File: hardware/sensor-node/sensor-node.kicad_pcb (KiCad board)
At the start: 2 copper layers, 70 x 70 mm, 46 parts, among them J1 Conn_ARM_JTAG_SWD_10, U1 AAT1217, U2 TPS27081A, U3 SHT31-DIS, U4 24LC32, U5 TSD305, U6 ADG633YCP, U7 TSV911RILT, U8 RFM95W, U9 STM32L412KB

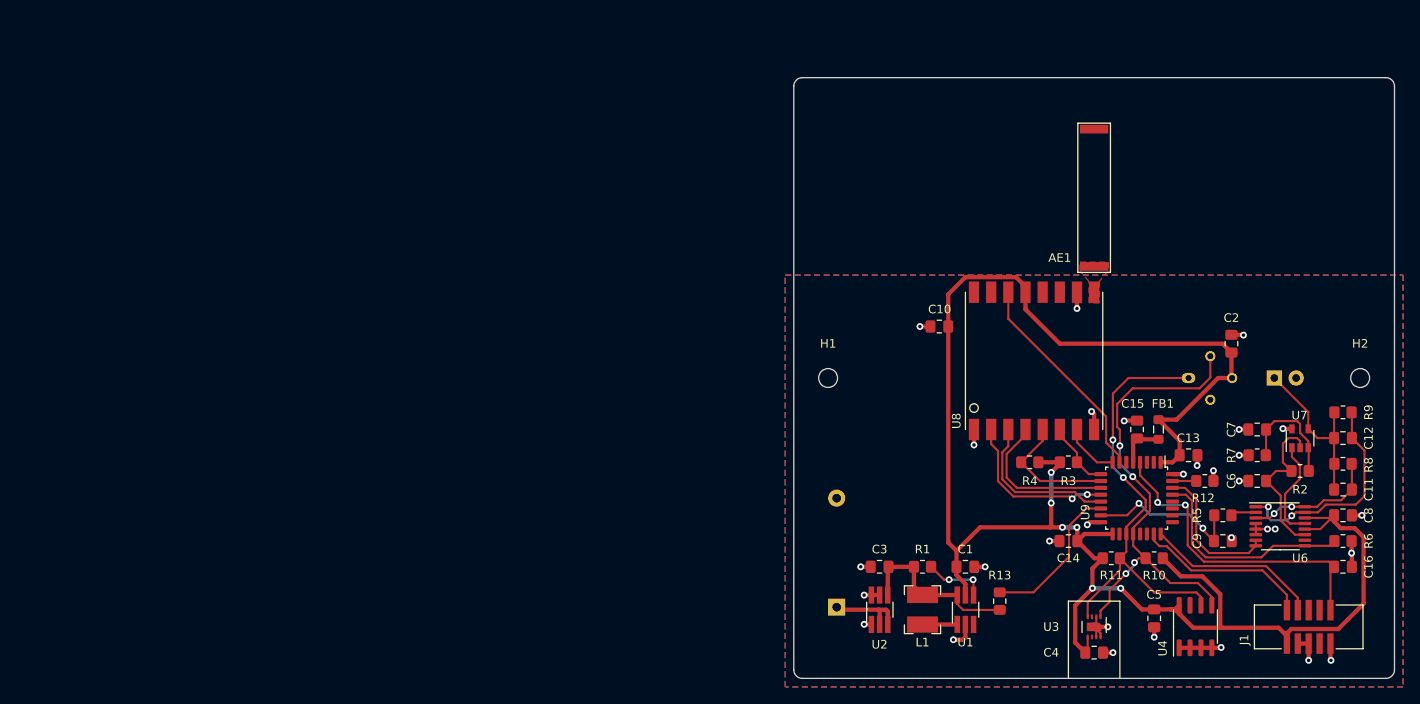
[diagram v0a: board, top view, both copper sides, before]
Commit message: Update PCB, add debugging printouts to application
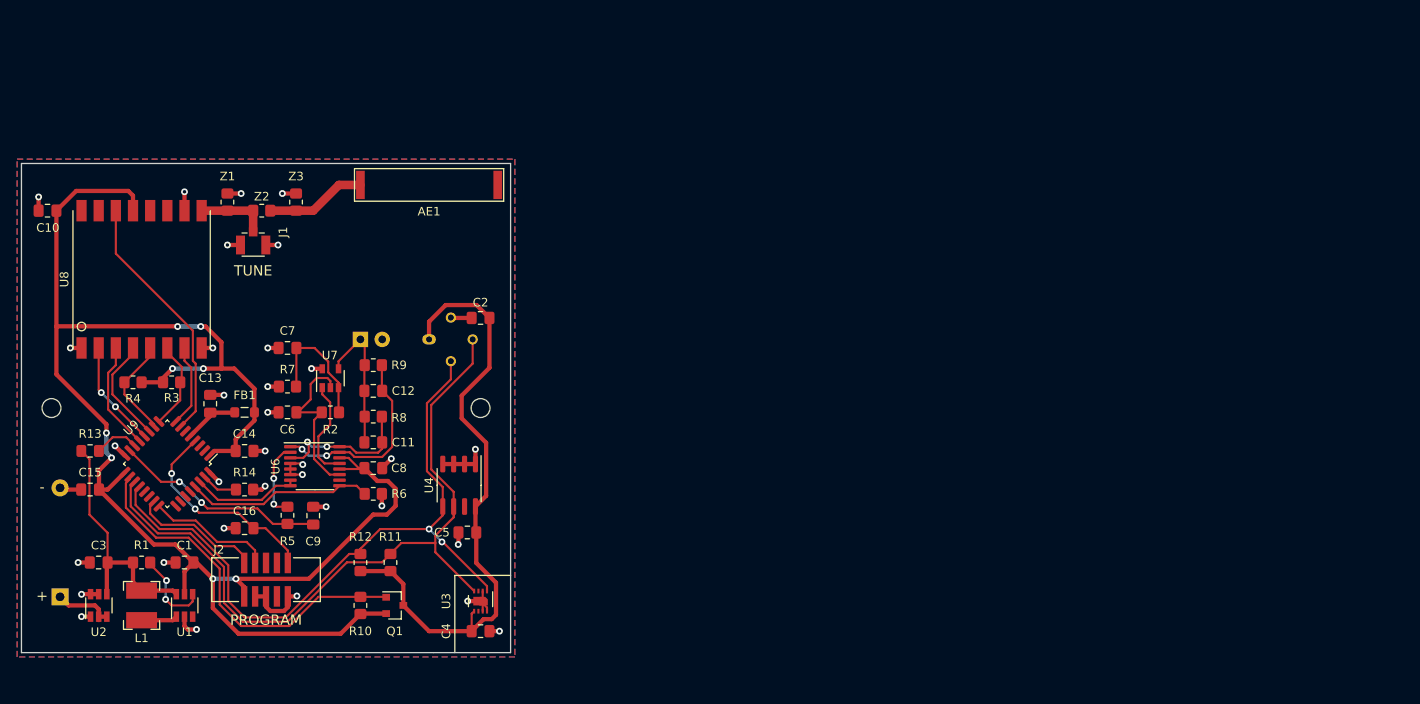
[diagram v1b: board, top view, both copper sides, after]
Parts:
- added J1: Conn_Coaxial, my-footprints-library:CONUFL001-SMD, F.Cu at (117.0, 69.5)
- added Q1: Q_PMOS_DGS, Package_TO_SOT_SMD:SOT-23, F.Cu at (133.5, 111.5)
- added R10: 100k, Resistor_SMD:R_0805_2012Metric_Pad1.20x1.40mm_HandSolder, F.Cu at (129.5, 111.5)
- added Z1: Z, Resistor_SMD:R_0805_2012Metric_Pad1.20x1.40mm_HandSolder, F.Cu at (114.0, 64.5)
- added Z2: Z, Resistor_SMD:R_0805_2012Metric_Pad1.20x1.40mm_HandSolder, F.Cu at (118.0, 65.5)
- added Z3: Z, Resistor_SMD:R_0805_2012Metric_Pad1.20x1.40mm_HandSolder, F.Cu at (122.0, 64.5)
- U1, U2: footprint Package_TO_SOT_SMD:TSOT-23-6_HandSoldering -> Package_TO_SOT_SMD:TSOT-23-6
- U5: value TSD305 -> MLX90614; footprint Package_TO_SOT_THT:TO-5-4_Window -> Package_TO_SOT_THT:TO-39-4
- moved C16 128.1 mm to (116.0, 102.5), turned to 180 degrees
- moved J2 121.6 mm to (118.5, 108.5)
- moved C15 114.2 mm to (98.0, 98.0)
- moved C7 113.4 mm to (121.0, 81.5)
- moved C6 113.3 mm to (121.0, 89.0)
- moved R7 113.3 mm to (121.0, 86.0)
- moved U7 113.2 mm to (126.0, 85.0)
- moved R2 113.2 mm to (126.0, 89.0)
- moved C11 113.1 mm to (131.0, 92.5)
- moved C12 113.1 mm to (131.0, 86.5)
- moved C8 113.1 mm to (131.0, 95.5)
- moved R6 113.1 mm to (131.0, 98.5)
- moved R8 113.1 mm to (131.0, 89.5)
- moved R9 113.1 mm to (131.0, 83.5)
- moved U9 113.0 mm to (107.0, 95.0), turned to 225 degrees
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- renumbered C15 to C13, C13 to C14, C14 to C15, J1 to J2, R10 to R11, R11 to R12, R12 to R14
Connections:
- C2 pad 1: +3V3 -> VI2C
- C4 pad 1: +3V3 -> VI2C
- C5 pad 1: +3V3 -> VI2C
- R11 pad 1: +3V3 -> VI2C
- R11 pad 2: SDA -> SCL
- R12 pad 1: +3V3 -> VI2C
- R12 pad 2: SCL -> SDA
- U3 pad 5: +3V3 -> VI2C
- U4 pad 8: +3V3 -> VI2C
- U5 pad 1: SCL -> VI2C
- U5 pad 2: SDA -> GND
- U5 pad 3: +3V3 -> SCL
- U5 pad 4: GND -> SDA
- U8 pad 9: Net-(AE1-Pad1) -> Net-(J1-Pad1)
- U9 pad 18: Net-(U9-Pad18) -> I2C_ENABLE
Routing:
- net VI2C: track 0.00 -> 72.5 mm
- net I2C_ENABLE: track 0.00 -> 43.7 mm
- net SCL: track 52.2 -> 86.5 mm, vias 2 -> 0
- net +3V3: track 218.7 -> 188.5 mm, vias 6 -> 8
- net SDA: track 55.6 -> 81.2 mm, vias 4 -> 2
- net GND: track 54.9 -> 70.5 mm, vias 31 -> 33
- net Net-(R13-Pad2): track 17.9 -> 5.25 mm
- net NRST: track 37.0 -> 24.4 mm
- net Net-(AE1-Pad1): track 0.00 -> 11.7 mm
- net Net-(J1-Pad1): track 0.00 -> 8.47 mm
- net VIN_SENSE: track 20.3 -> 28.5 mm
- net MISO: track 19.4 -> 12.5 mm
- net PHOTO_SENSE: track 18.9 -> 24.9 mm
- net MOSI: track 18.6 -> 12.7 mm
- net SWCLK: track 20.5 -> 14.8 mm
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- removed copper zone on F.Cu, net Net-(AE1-Pad1)
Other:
- board size 70 x 70 mm -> 57 x 57 mm
- board text added: "+"
- board text added: "-"
- board text added: "PROGRAM"
- board text added: "TUNE"

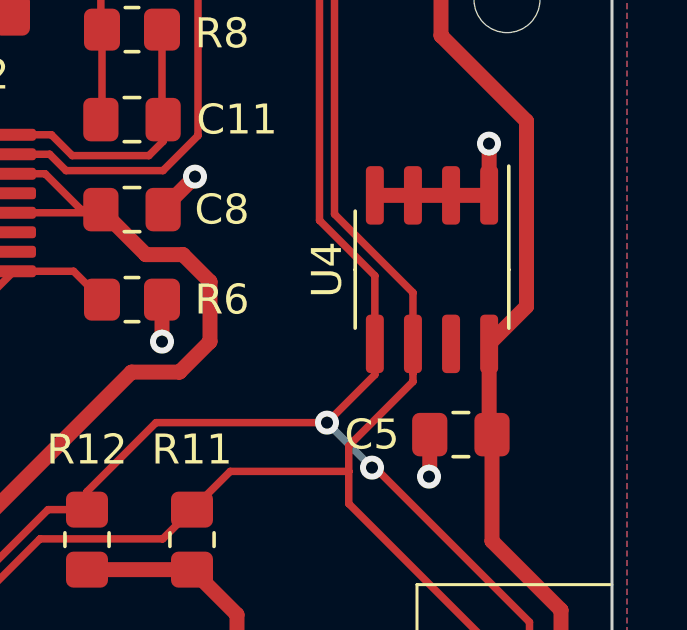
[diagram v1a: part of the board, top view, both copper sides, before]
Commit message: Fix timeouts for systick overflow handling
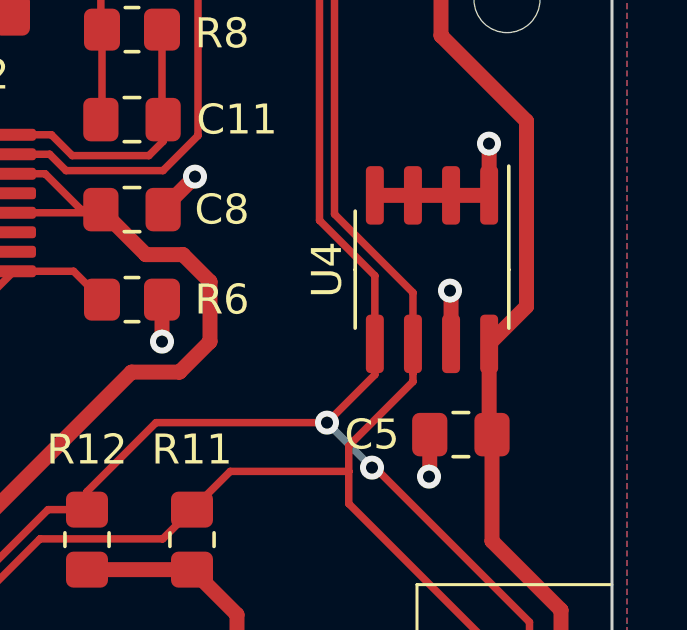
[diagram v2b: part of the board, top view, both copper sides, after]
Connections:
- U4 pad 7: Net-(U4-Pad7) -> GND
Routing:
- net GND: track 70.5 -> 72.3 mm, vias 33 -> 34

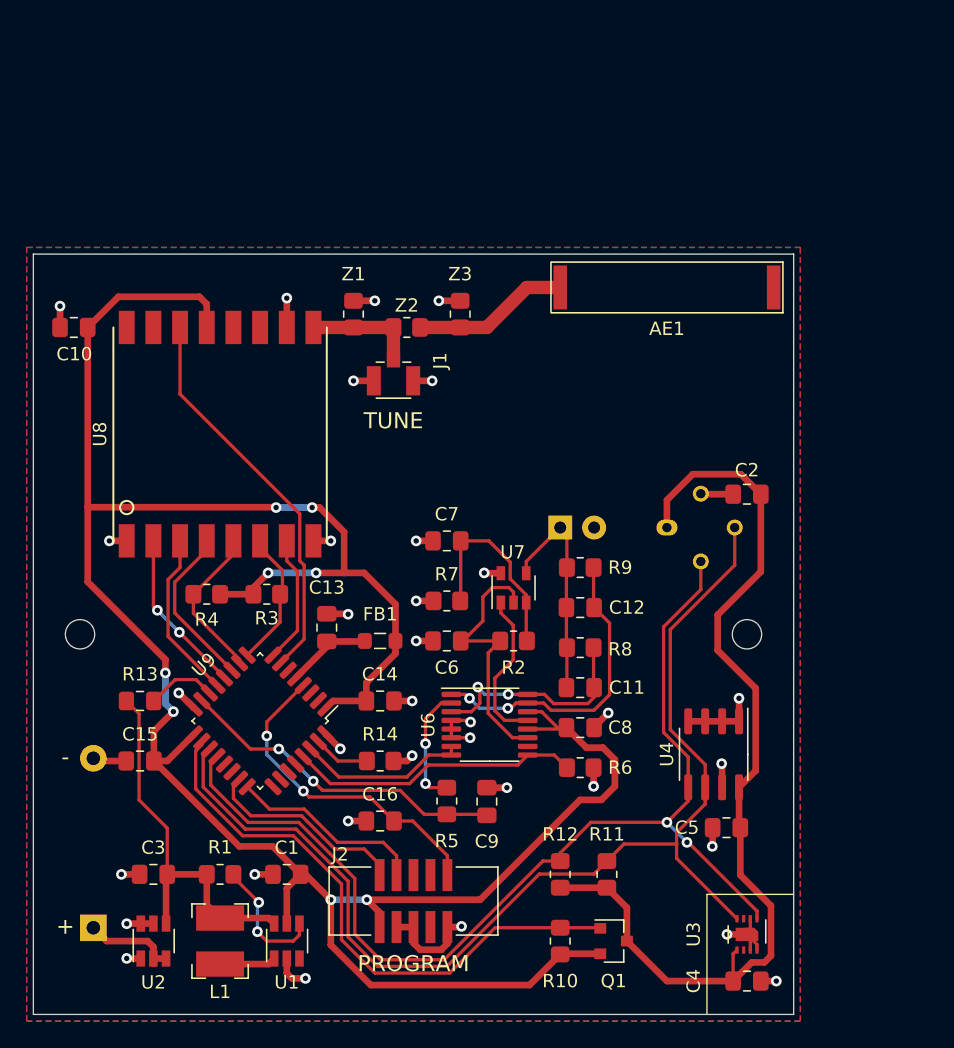
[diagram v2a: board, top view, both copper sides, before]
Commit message: Update PCB for enclosure
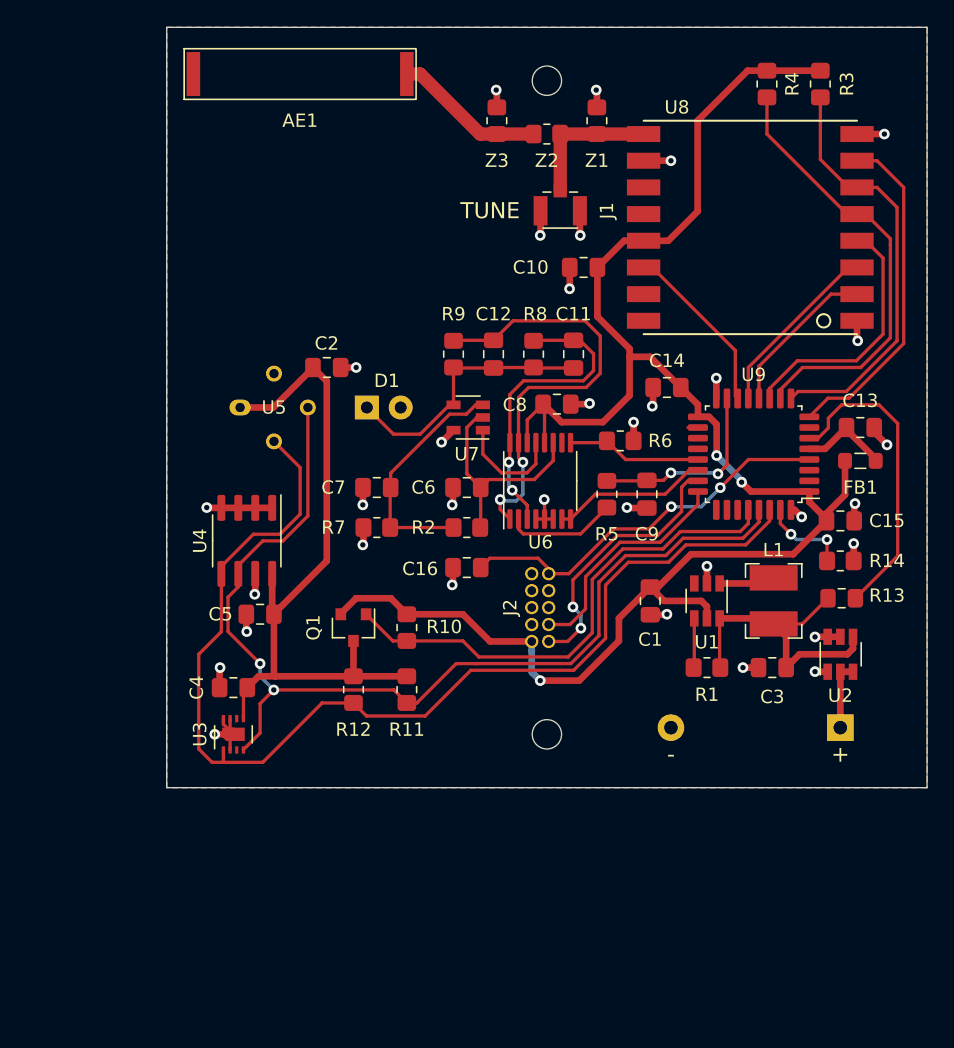
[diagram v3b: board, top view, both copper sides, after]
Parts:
- FB1: value Ferrite_Bead_Small -> WE 742792040
- J1: value Conn_Coaxial -> CONUFL001-SMD-T
- J2: footprint my-footprints-library:Amphenol_FCI_ShroudedSocket_2x05_P1.27mm_Vertical_SMD -> my-footprints-library:SHF-105-01-L-D-TH; moved to B.Cu
- Q1: value Q_PMOS_DGS -> PMV250EPEA
- moved BT1 58.0 mm to (150.5, 95.5), turned to 90 degrees
- moved R4 56.8 mm to (145.0, 47.2), turned to 270 degrees
- moved R3 56.4 mm to (149.0, 47.2), turned to 270 degrees
- moved U2 55.8 mm to (150.5, 90.0)
- moved C15 55.5 mm to (150.5, 80.0), turned to 0 degrees
- moved R13 53.2 mm to (150.6, 85.8)
- moved C3 48.9 mm to (145.4, 91.0)
- moved L1 48.7 mm to (145.5, 86.0), turned to 270 degrees
- moved C4 44.3 mm to (105.0, 92.5), turned to 180 degrees
- moved H2 44.1 mm to (128.5, 47.0)
- moved C13 42.7 mm to (152.0, 73.0), turned to 0 degrees
- moved U8 42.7 mm to (143.8, 58.0), turned to 180 degrees
- moved U9 42.1 mm to (144.0, 75.0), turned to 180 degrees
- moved U3 41.3 mm to (105.0, 96.0), turned to 90 degrees
- moved U1 40.5 mm to (140.5, 86.0), turned to 270 degrees
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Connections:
- U9 pad 14: Net-(R13-Pad2) -> RFM95_IRQ
- U9 pad 18: I2C_ENABLE -> Net-(U9-Pad18)
- U9 pad 19: SCL -> Net-(U9-Pad19)
- U9 pad 20: SDA -> Net-(U9-Pad20)
- U9 pad 21: Net-(U9-Pad21) -> PHOTO_ENABLE
- U9 pad 22: Net-(U9-Pad22) -> PHOTO_SWITCH
- U9 pad 28: Net-(U9-Pad28) -> I2C_ENABLE
- U9 pad 29: PHOTO_ENABLE -> SCL
- U9 pad 30: PHOTO_SWITCH -> SDA
- U9 pad 6: Net-(U9-Pad6) -> Net-(R13-Pad2)
- U9 pad 7: RFM95_IRQ -> Net-(U9-Pad7)
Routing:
- net +3V3: track 188.5 -> 131.6 mm, vias 8 -> 3
- net RFM95_NRST: track 10.4 -> 31.6 mm
- net RFM95_NSS: track 12.4 -> 33.2 mm
- net VI2C: track 72.5 -> 52.5 mm
- net Net-(R13-Pad2): track 5.25 -> 23.1 mm
- net RFM95_IRQ: track 29.7 -> 13.1 mm
- net RFM95_DIO5: track 9.66 -> 25.4 mm
- net GND: track 72.3 -> 58.1 mm
- net PHOTO_ENABLE: track 21.9 -> 10.2 mm
- net PHOTO_SENSE: track 24.9 -> 14.5 mm
- net Net-(C12-Pad2): track 23.2 -> 32.9 mm
- net SCL: track 86.5 -> 77.1 mm, vias 0 -> 2
- net SCK: track 12.5 -> 19.1 mm
- net Net-(C11-Pad2): track 16.8 -> 23.2 mm
- net Net-(R1-Pad2): track 10.0 -> 3.71 mm, vias 2 -> 0
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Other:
- outline, holes or cut-outs redrawn
- board text added: "FLASH"
- board text removed: "PROGRAM"
